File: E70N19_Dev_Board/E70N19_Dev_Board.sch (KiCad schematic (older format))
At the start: 63 parts, among them J1 USB_OTG, J2 Battery 1x2, J3 JTAGSEL_JUMPER 1x3, J4 UART_PROG 1x2, J5 ERASE_JUMPER 1x3, J6 ARM-Cortex-Debug-10, J7 CAN 1x2, J8 Conn_02x15_Counter_Clockwise, J9 Conn_02x15_Counter_Clockwise, SW1 NRST_BUTTON, U1 MCP73831, U2 TPS2112A, U3 SPX3819M5-L-3-3, U4 ATSAME70N19, U5 RT9818A-18GV, U6 SN65HVD233-Q1, Y1 Crystal_GND23_Small, Y2 Crystal

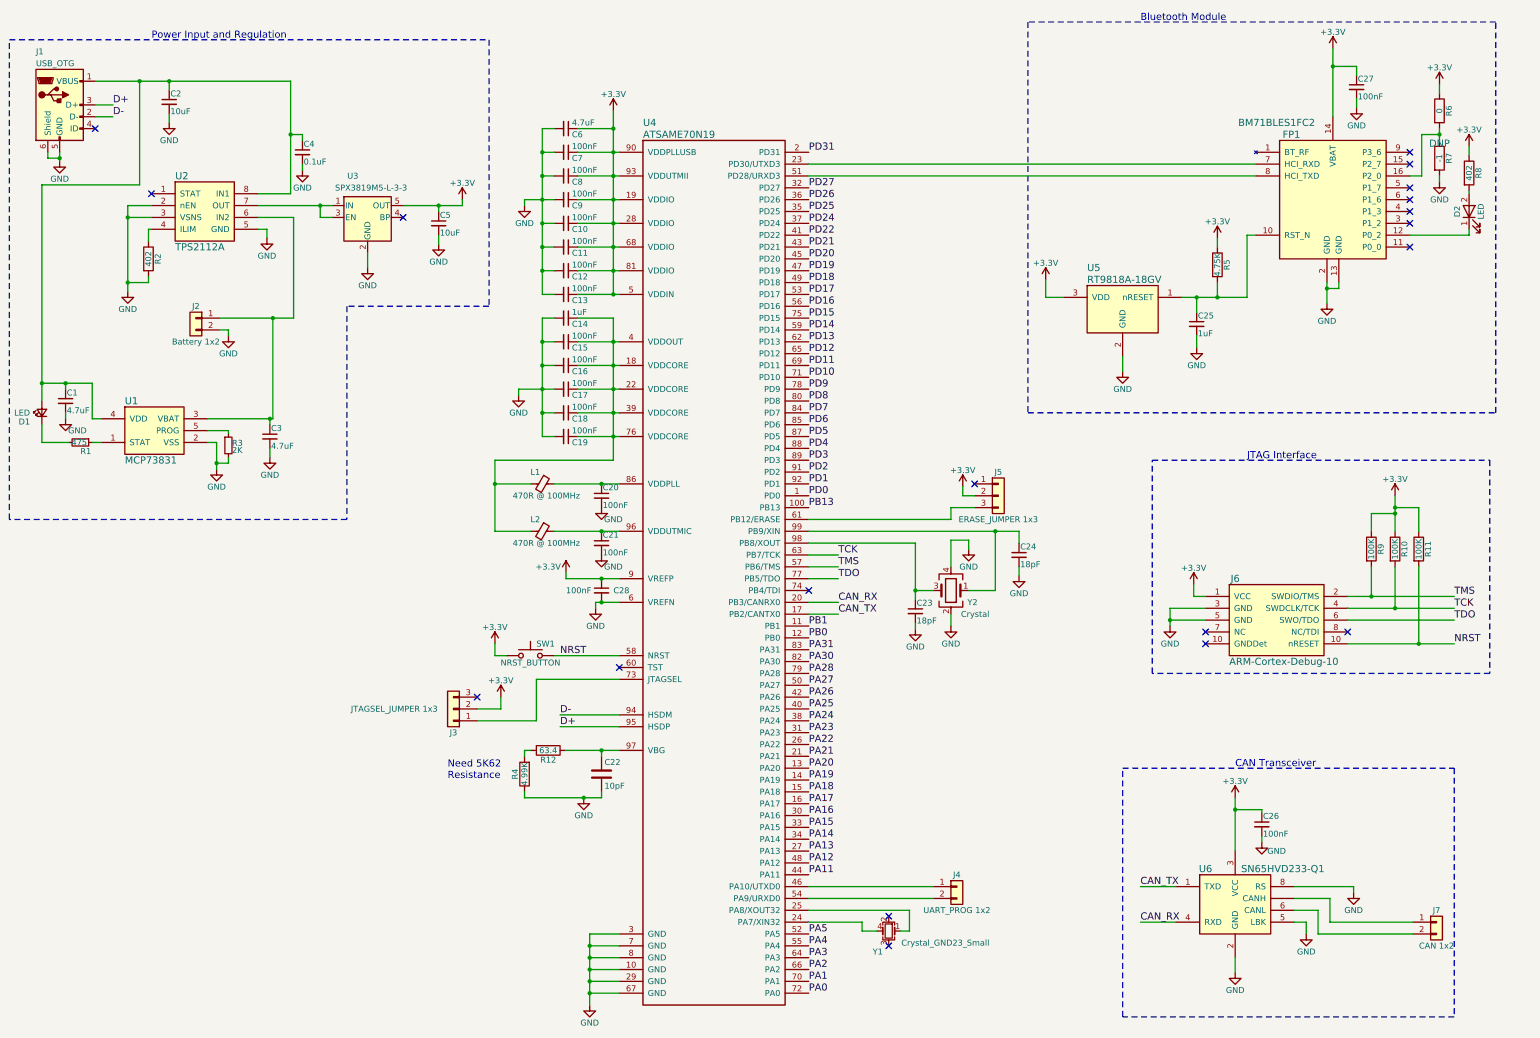
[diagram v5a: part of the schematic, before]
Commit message: Fixing up schematic based on design review notes
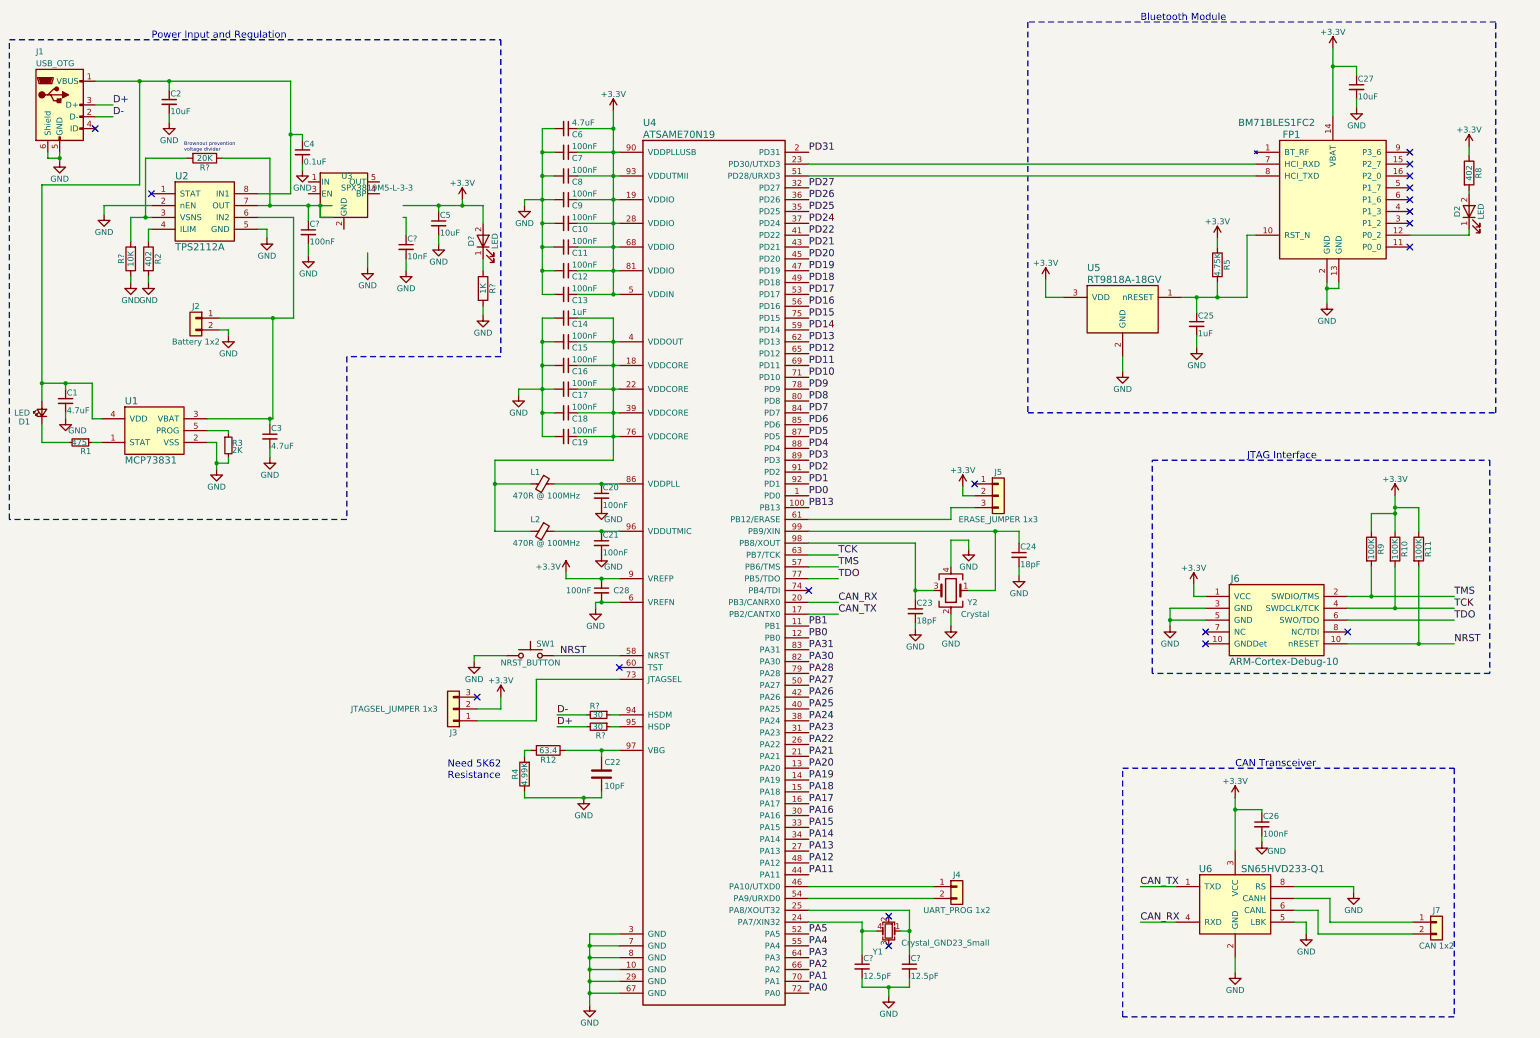
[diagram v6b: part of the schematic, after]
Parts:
- removed R6: 0, symbol R
- removed R7: -1, symbol R
- added C?: 10nF, symbol C_Small
- added C?: 100nF, symbol C_Small
- added C? (x2): 12.5pF, symbol C_Small
- added D?: LED, symbol LED
- added R?: 1K, symbol R
- added R? (x2): 30, symbol R_Small
- added R?: 20K, symbol R
- added R?: 10K, symbol R
- C27: value 100nF -> 10uF
- U2, U3: Fieldname (none) -> Value
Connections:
- net +3V3: now also D?.2 (A); no longer SW1.1, U3.5 (OUT)
- net D+: now also R?.2; no longer U4.95 (HSDP)
- net D-: now also R?.2; no longer U4.94 (HSDM)
- net GND: now also SW1.1, C?.2, C?.2, C?.2, C?.2, R?.1, R?.2; no longer U2.3 (VSNS), U3.2 (GND)
- net at U4.24 (PA7/XIN32), Y1.4: now also C?.1
- net at U4.25 (PA8/XOUT32), Y1.1: now also C?.1
- new net: R?.1, U4.94 (HSDM)
- new net: R?.1, U4.95 (HSDP)
- new net: R?.2, R?.2, U2.3 (VSNS)
- new net: C?.1, R?.1, U2.7 (OUT)
- new net: D?.1 (K), R?.1
- now unconnected: U3.1 (IN), U3.3 (EN)
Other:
- note added: "Brownout prevention\nvoltage divider\n"
- moved on the sheet: U3

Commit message: Hoppe did not save correctly
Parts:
- C1, C10, C11, C12, C13, C14, C15, C16, C17, C18, C19, C20, C21, C22, C23, C24, C25, C26, C28, C3, C4, C6, C7, C8, C9: footprint (none) -> Capacitors_SMD:C_0603
- C2, C27, C5: footprint (none) -> Capacitors_SMD:C_0805
- C29, C30, C31, C32: renamed from C?; footprint (none) -> Capacitors_SMD:C_0603
- D1: footprint (none) -> LEDs:LED_0805
- D2: footprint (none) -> LEDs:LED_0805; symbol LED -> LED-RESCUE-E70N19_Dev_Board
- D3: renamed from D?; footprint (none) -> LEDs:LED_0805; symbol LED -> LED-RESCUE-E70N19_Dev_Board
- J1: footprint (none) -> Connect:USB_Micro-B; symbol USB_OTG -> USB_OTG-RESCUE-E70N19_Dev_Board
- gave numbers to parts that had none: 5
